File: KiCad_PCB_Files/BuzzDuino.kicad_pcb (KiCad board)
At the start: 2 copper layers, 76.2 x 53.3 mm, 22 parts, among them J1 Conn_01x02_Female, J2 Wire, U1 74HC595, U2 HDSP-A151

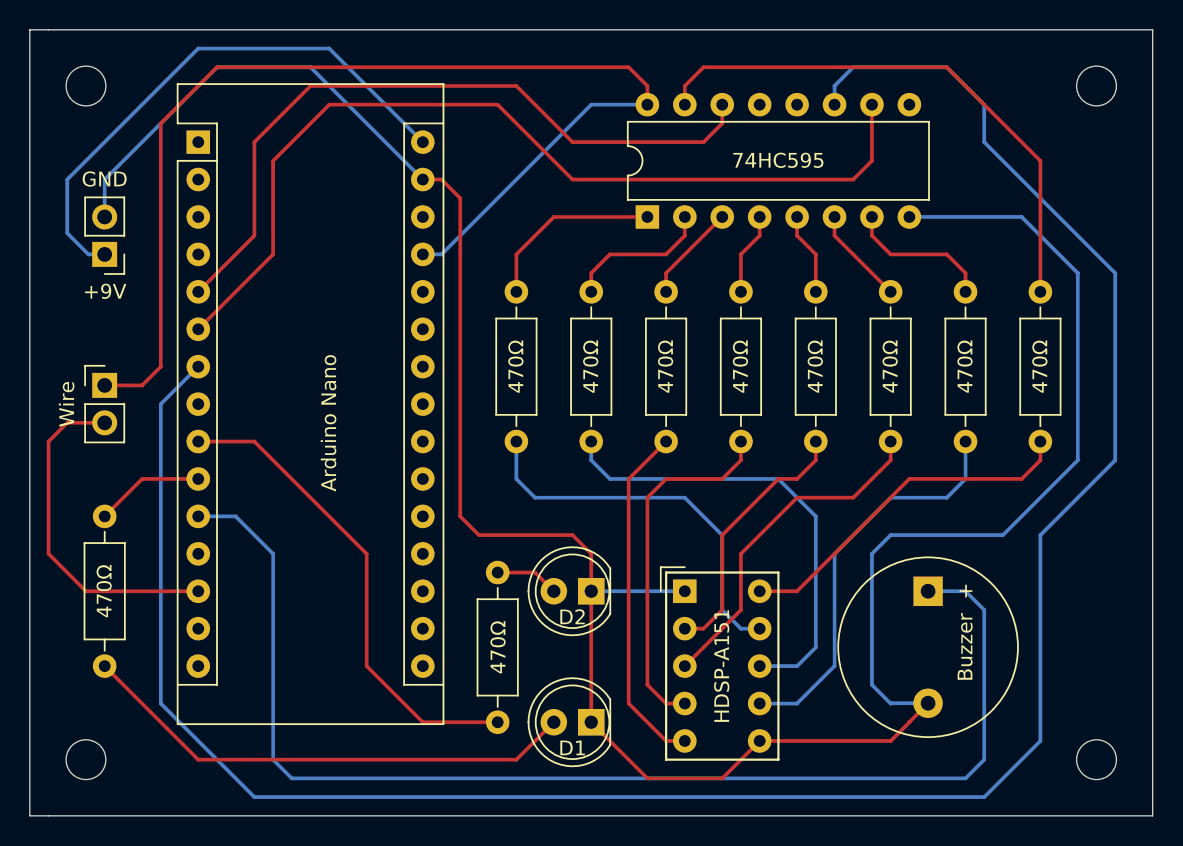
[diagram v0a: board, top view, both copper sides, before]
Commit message: use correct IC pins
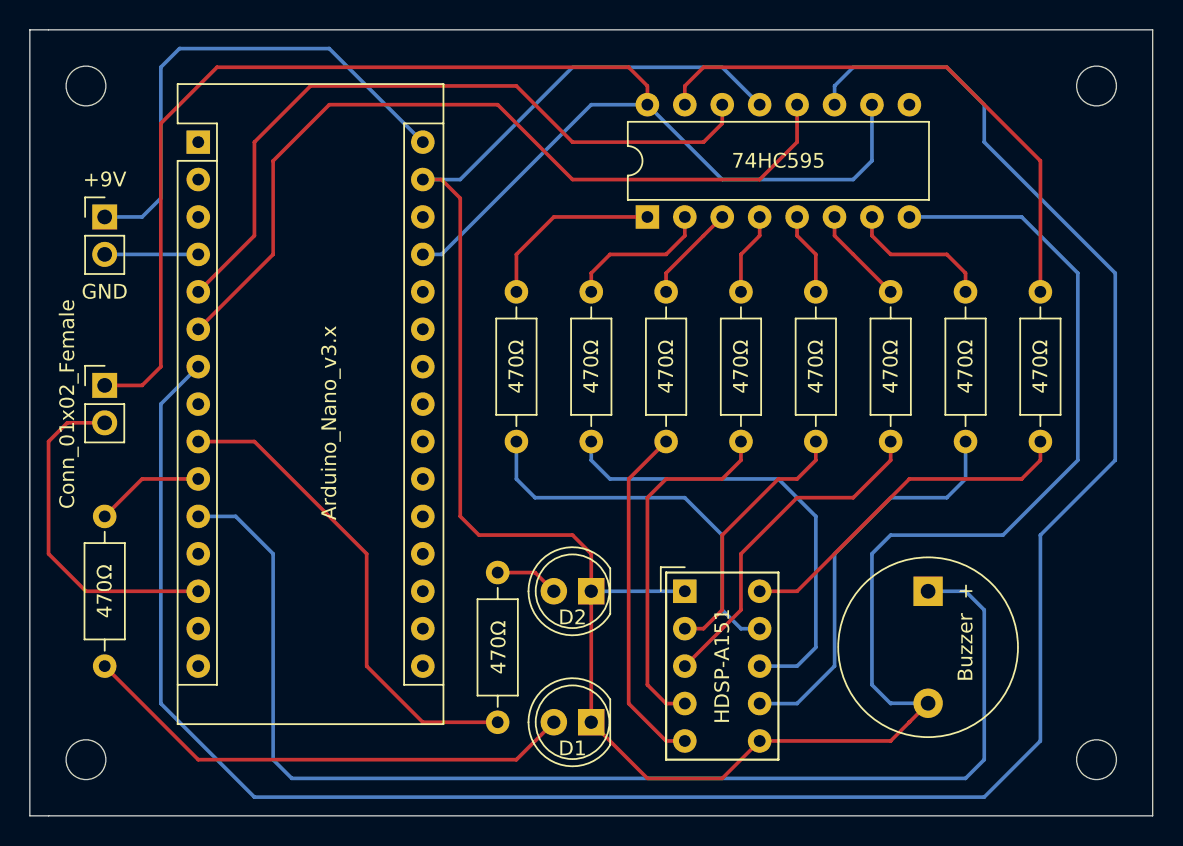
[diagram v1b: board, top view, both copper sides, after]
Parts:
- A1: value Arduino Nano -> Arduino_Nano_v3.x
- J2: value Wire -> Conn_01x02_Female
- moved J1 2.54 mm to (101.6, 85.1), turned to 0 degrees
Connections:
- J1 pad 2: GND -> Net-(A1-Pad4)
- U1 pad 10: Net-(A1-Pad6) -> /5V
- U1 pad 12: Net-(U1-Pad12) -> Net-(A1-Pad6)
- U1 pad 13: Net-(U1-Pad13) -> GND
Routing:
- net /5V: track 76.7 -> 98.4 mm
- net Net-(A1-Pad4): track 0.00 -> 6.35 mm
- net Net-(A1-Pad6): track 62.2 -> 56.4 mm
- net GND: track 164.9 -> 161.6 mm
- net +9V: track 37.2 -> 34.2 mm

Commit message: using plated mounting holes
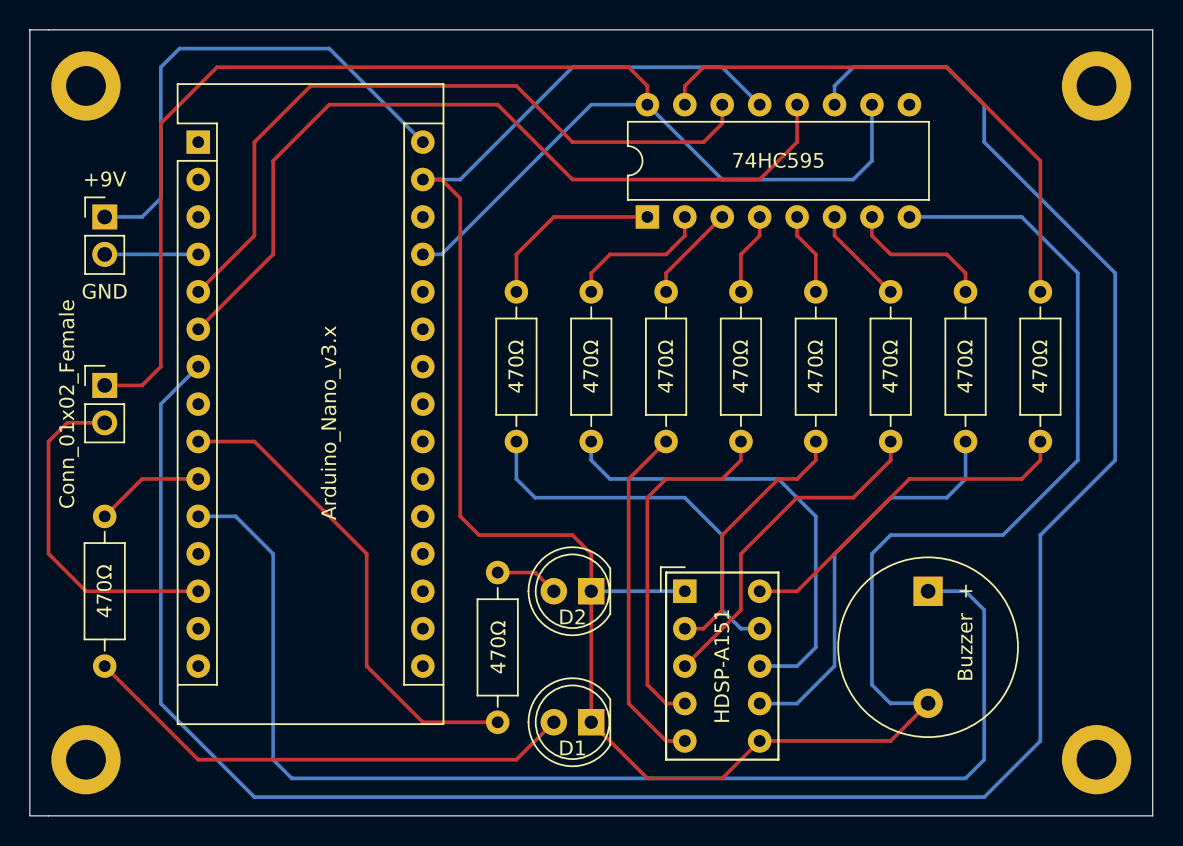
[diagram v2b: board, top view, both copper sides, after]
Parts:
- removed the ? at (100.3, 76.2)
- removed the ? at (100.3, 121.9)
- removed the ? at (168.9, 76.2)
- removed the ? at (168.9, 121.9)
- added ?: M2.5_DIN965_Pad, MountingHole:MountingHole_2.7mm_M2.5_DIN965_Pad, F.Cu at (100.3, 76.2)
- added ?: M2.5_DIN965_Pad, MountingHole:MountingHole_2.7mm_M2.5_DIN965_Pad, F.Cu at (100.3, 121.9)
- added ?: M2.5_DIN965_Pad, MountingHole:MountingHole_2.7mm_M2.5_DIN965_Pad, F.Cu at (168.9, 121.9)
- added ?: M2.5_DIN965_Pad, MountingHole:MountingHole_2.7mm_M2.5_DIN965_Pad, F.Cu at (168.9, 76.2)
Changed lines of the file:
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@@
     (add_net "Net-(U1-Pad9)")
+  )
+  (module MountingHole:MountingHole_2.7mm_M2.5_DIN965_Pad (layer F.Cu)
+    (at 100.33 76.2)
+    (descr "Mounting Hole 2.7mm, M2.5, DIN965")
+    (tags "mounting hole 2.7mm m2.5 din965")
+    (attr virtual)
+    (fp_text reference "" (at 0 -3.35) (layer F.Fab)
+      (effects (font (size 1 1) (thickness 0.15)))
+    )
+    (fp_text value M2.5_DIN965_Pad (at 2.54 -5.08) (layer F.Fab)
+      (effects (font (size 1 1) (thickness 0.15)))
+    )
+    (fp_circle (center 0 0) (end 2.35 0) (layer Cmts.User) (width 0.15))
+    (fp_circle (center 0 0) (end 2.6 0) (layer F.CrtYd) (width 0.05))
+    (pad 1 thru_hole circle (at 0 0) (size 4.7 4.7) (drill 2.7) (layers *.Cu *.Mask))
+  )
+  (module MountingHole:MountingHole_2.7mm_M2.5_DIN965_Pad (layer F.Cu)
+    (at 100.33 121.92)
+    (descr "Mounting Hole 2.7mm, M2.5, DIN965")
+    (tags "mounting hole 2.7mm m2.5 din965")
+    (attr virtual)
+    (fp_text reference "" (at 0 -3.35) (layer F.Fab)
+      (effects (font (size 1 1) (thickness 0.15)))
+    )
+    (fp_text value M2.5_DIN965_Pad (at 2.54 5.08) (layer F.Fab)
+      (effects (font (size 1 1) (thickness 0.15)))
+    )
+    (fp_circle (center 0 0) (end 2.35 0) (layer Cmts.User) (width 0.15))
+    (fp_circle (center 0 0) (end 2.6 0) (layer F.CrtYd) (width 0.05))
+    (pad 1 thru_hole circle (at 0 0) (size 4.7 4.7) (drill 2.7) (layers *.Cu *.Mask))
+  )
+  (module MountingHole:MountingHole_2.7mm_M2.5_DIN965_Pad (layer F.Cu)
+    (at 168.91 121.92)
+    (descr "Mounting Hole 2.7mm, M2.5, DIN965")
+    (tags "mounting hole 2.7mm m2.5 din965")
+    (attr virtual)
+    (fp_text reference "" (at 0 -3.35) (layer F.Fab)
+      (effects (font (size 1 1) (thickness 0.15)))
+    )
+    (fp_text value M2.5_DIN965_Pad (at -2.54 6.35) (layer F.Fab)
+      (effects (font (size 1 1) (thickness 0.15)))
+    )
+    (fp_circle (center 0 0) (end 2.35 0) (layer Cmts.User) (width 0.15))
+    (fp_circle (center 0 0) (end 2.6 0) (layer F.CrtYd) (width 0.05))
+    (pad 1 thru_hole circle (at 0 0) (size 4.7 4.7) (drill 2.7) (layers *.Cu *.Mask))
+  )
+  (module MountingHole:MountingHole_2.7mm_M2.5_DIN965_Pad (layer F.Cu)
+    (at 168.91 76.2)
+    (descr "Mounting Hole 2.7mm, M2.5, DIN965")
+    (tags "mounting hole 2.7mm m2.5 din965")
+    (attr virtual)
+    (fp_text reference "" (at 0 -3.35) (layer F.Fab)
+      (effects (font (size 1 1) (thickness 0.15)))
+    )
+    (fp_text value M2.5_DIN965_Pad (at -2.54 -5.08) (layer F.Fab)
+      (effects (font (size 1 1) (thickness 0.15)))
+    )
+    (fp_circle (center 0 0) (end 2.6 0) (layer F.CrtYd) (width 0.05))
+    (fp_circle (center 0 0) (end 2.35 0) (layer Cmts.User) (width 0.15))
+    (pad 1 thru_hole circle (at 0 0) (size 4.7 4.7) (drill 2.7) (layers *.Cu *.Mask))
   )
   (module Package_DIP:DIP-16_W7.62mm (layer F.Cu)
@@
     )
   )
-  (module MountingHole:MountingHole_2.7mm_M2.5 (layer F.Cu)
-    (at 100.33 76.2)
-    (descr "Mounting Hole 2.7mm, no annular, M2.5")
-    (tags "mounting hole 2.7mm no annular m2.5")
-    (attr virtual)
-    (fp_text reference "" (at 0 -3.7) (layer F.SilkS)
-      (effects (font (size 1 1) (thickness 0.15)))
-    )
-    (fp_text value MountingHole_2.7mm_M2.5 (at 0 -5.08) (layer F.Fab)
-      (effects (font (size 1 1) (thickness 0.15)))
-    )
-    (fp_text user %R (at 0.3 0) (layer F.Fab)
-      (effects (font (size 1 1) (thickness 0.15)))
-    )
-    (fp_circle (center 0 0) (end 2.7 0) (layer Cmts.User) (width 0.15))
-    (fp_circle (center 0 0) (end 2.95 0) (layer F.CrtYd) (width 0.05))
-    (pad 1 np_thru_hole circle (at 0 0) (size 2.7 2.7) (drill 2.7) (layers *.Cu *.Mask))
-  )
-  (module MountingHole:MountingHole_2.7mm_M2.5 (layer F.Cu)
-    (at 100.33 121.92)
-    (descr "Mounting Hole 2.7mm, no annular, M2.5")
-    (tags "mounting hole 2.7mm no annular m2.5")
-    (attr virtual)
-    (fp_text reference "" (at -1.27 -5.08) (layer F.SilkS)
-      (effects (font (size 1 1) (thickness 0.15)))
-    )
-    (fp_text value MountingHole_2.7mm_M2.5 (at 0 5.08) (layer F.Fab)
-      (effects (font (size 1 1) (thickness 0.15)))
-    )
-    (fp_text user %R (at 0.3 0) (layer F.Fab)
-      (effects (font (size 1 1) (thickness 0.15)))
-    )
-    (fp_circle (center 0 0) (end 2.7 0) (layer Cmts.User) (width 0.15))
-    (fp_circle (center 0 0) (end 2.95 0) (layer F.CrtYd) (width 0.05))
-    (pad 1 np_thru_hole circle (at 0 0) (size 2.7 2.7) (drill 2.7) (layers *.Cu *.Mask))
-  )
-  (module MountingHole:MountingHole_2.7mm_M2.5 (layer F.Cu)
-    (at 168.91 76.2)
-    (descr "Mounting Hole 2.7mm, no annular, M2.5")
-    (tags "mounting hole 2.7mm no annular m2.5")
-    (attr virtual)
-    (fp_text reference "" (at 0 -3.7) (layer F.SilkS)
-      (effects (font (size 1 1) (thickness 0.15)))
-    )
-    (fp_text value MountingHole_2.7mm_M2.5 (at -3.81 -5.08) (layer F.Fab)
-      (effects (font (size 1 1) (thickness 0.15)))
-    )
-    (fp_text user %R (at 0.3 0) (layer F.Fab)
-      (effects (font (size 1 1) (thickness 0.15)))
-    )
-    (fp_circle (center 0 0) (end 2.7 0) (layer Cmts.User) (width 0.15))
-    (fp_circle (center 0 0) (end 2.95 0) (layer F.CrtYd) (width 0.05))
-    (pad 1 np_thru_hole circle (at 0 0) (size 2.7 2.7) (drill 2.7) (layers *.Cu *.Mask))
-  )
-  (module MountingHole:MountingHole_2.7mm_M2.5 (layer F.Cu)
-    (at 168.91 121.92)
-    (descr "Mounting Hole 2.7mm, no annular, M2.5")
-    (tags "mounting hole 2.7mm no annular m2.5")
-    (attr virtual)
-    (fp_text reference "" (at 0 -3.7) (layer F.SilkS)
-      (effects (font (size 1 1) (thickness 0.15)))
-    )
-    (fp_text value MountingHole_2.7mm_M2.5 (at 0 5.08) (layer F.Fab)
-      (effects (font (size 1 1) (thickness 0.15)))
-    )
-    (fp_circle (center 0 0) (end 2.95 0) (layer F.CrtYd) (width 0.05))
-    (fp_circle (center 0 0) (end 2.7 0) (layer Cmts.User) (width 0.15))
-    (fp_text user %R (at 0.3 0) (layer F.Fab)
-      (effects (font (size 1 1) (thickness 0.15)))
-    )
-    (pad 1 np_thru_hole circle (at 0 0) (size 2.7 2.7) (drill 2.7) (layers *.Cu *.Mask))
-  )
   (module Resistor_THT:R_Axial_DIN0207_L6.3mm_D2.5mm_P10.16mm_Horizontal (layer F.Cu)
